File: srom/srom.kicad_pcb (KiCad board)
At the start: 2 copper layers, 116.8 x 118.9 mm, 99 parts, among them J1 Conn_01x03_Female, J201 Conn_01x03_Female, J301 Conn_01x05_Female, J302 Conn_01x04_Female, J303 Conn_01x03_Female, Q1 PMBT2222A, U1 4075, U2 74LS245, U201 Pico-2 IO, U202 74LS245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

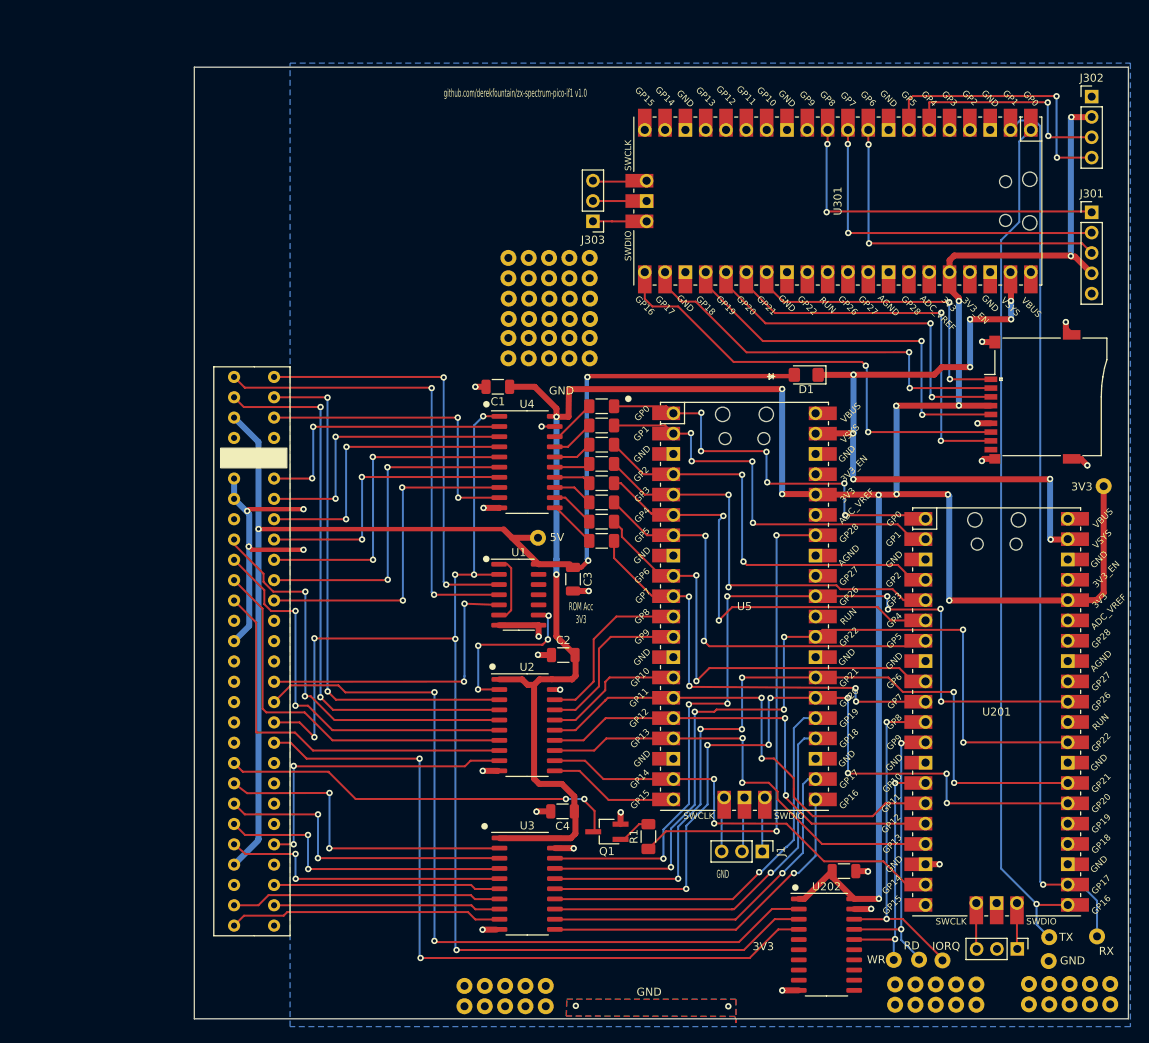
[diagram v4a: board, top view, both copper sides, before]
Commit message: update schema and layout to match working ROM emulation board. 2 level shifters removed here
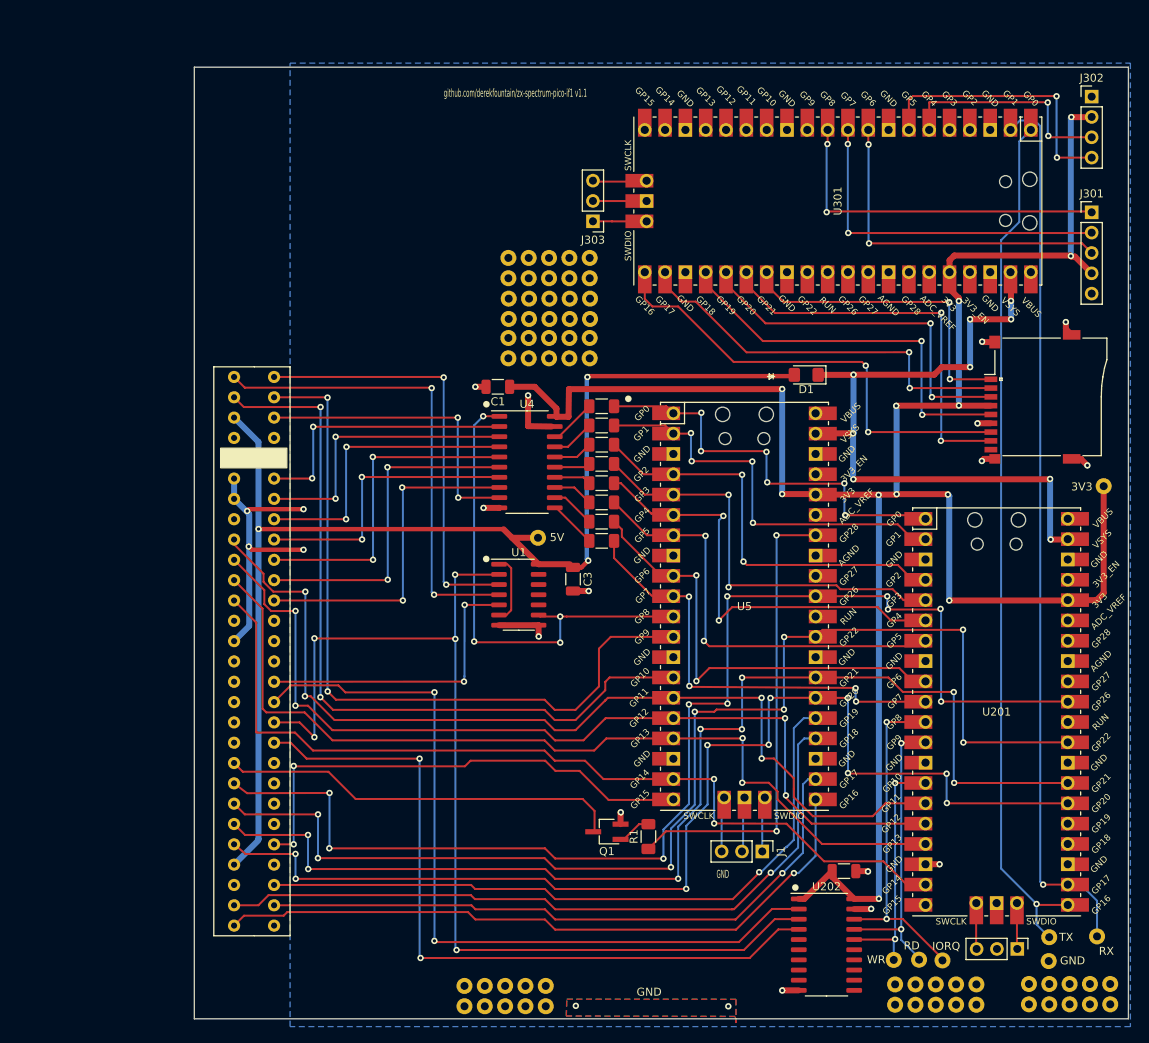
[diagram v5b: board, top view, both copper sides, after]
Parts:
- removed C2, C4: C_Small, Capacitor_SMD:C_1206_3216Metric
- removed U2, U3: 74LS245, Package_SO:SO-20_5.3x12.6mm_P1.27mm
- R101, R102, R103, R104, R105, R106, R107, R108: value R470 -> R150
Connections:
- U201 pad 15: A0 -> ZXA0
- U201 pad 16: A1 -> ZXA1
- U201 pad 17: A2 -> ZXA2
- U201 pad 19: A3 -> ZXA3
- U201 pad 26: A4 -> ZXA4
- U201 pad 27: A5 -> ZXA5
- U201 pad 29: A6 -> ZXA6
- U201 pad 31: A7 -> ZXA7
- U4 pad 1: ZXRD -> ROM_READ_INV
- U5 pad 11: ROM_READ_INV_3V3 -> ROM_READ_INV
- U5 pad 12: A13 -> ZXA13
- U5 pad 14: A12 -> ZXA12
- U5 pad 15: A0 -> ZXA0
- U5 pad 16: A1 -> ZXA1
- U5 pad 17: A2 -> ZXA2
- U5 pad 19: A3 -> ZXA3
- U5 pad 20: M1 -> ZXM1
- U5 pad 21: A11 -> ZXA11
- U5 pad 22: A10 -> ZXA10
- U5 pad 24: A9 -> ZXA9
- U5 pad 25: A8 -> ZXA8
- U5 pad 26: A4 -> ZXA4
- U5 pad 27: A5 -> ZXA5
- U5 pad 29: A6 -> ZXA6
- U5 pad 31: A7 -> ZXA7
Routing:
- net ZXA7: track 40.2 -> 156.2 mm, vias 2 -> 10
- net ZXA6: track 38.8 -> 152.2 mm, vias 2 -> 8
- net A7: track 108.1 -> 0.00 mm, vias 8 -> 0
- net ZXA5: track 37.6 -> 145.1 mm, vias 2 -> 8
- net ZXA4: track 36.3 -> 143.6 mm, vias 2 -> 10
- net A6: track 105.5 -> 0.00 mm, vias 6 -> 0
- net A5: track 99.7 -> 0.00 mm, vias 6 -> 0
- net A4: track 99.4 -> 0.00 mm, vias 8 -> 0
- net +3V3: track 337.3 -> 261.8 mm, vias 14 -> 12
- net ZXA0: track 50.4 -> 118.8 mm, vias 2 -> 4
- net ZXA1: track 49.8 -> 116.1 mm, vias 2 -> 4
- net ZXA2: track 48.6 -> 112.6 mm, vias 0 -> 2
- net ZXA3: track 48.7 -> 110.0 mm, vias 0 -> 2
- net A0: track 60.7 -> 0.00 mm, vias 2 -> 0
- net A1: track 58.7 -> 0.00 mm, vias 2 -> 0
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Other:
- board text added: "github.com/derekfountain/zx-spectrum-pico-if1 v1.1"
- board text removed: "ROM Acc 3V3"
- board text removed: "github.com/derekfountain/zx-spectrum-pico-if1 v1.0"
